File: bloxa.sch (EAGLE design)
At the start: 87 parts, among them CON1 PINHEAD_1X02-2.54, CON7 CON-4P-JST_GH-RA, CON8 CON-4P-JST_GH-RA, IC1 TPD3S014DBVR-SOT23-6, IC3 TJA1051, IC6 MCP9700, Q13 BUK9K6R2-40E,115, Q14 BUK9K6R2-40E,115, Q15 BUK9K6R2-40E,115

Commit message: updates
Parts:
- removed PAD42, PAD43: PAD-4X2, PADS:PAD-4X2
- added BAT+, BAT-: PAD-4X2, PADS:PAD-4X2
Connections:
- removed net CAN2_LED1: R9.1
- removed net LED_BLUE: R11.2
- removed net LED_GREEN: R12.2
- removed net LED_RED: R13.2
- removed net N$3: D1.C, D2.C, PAD43.P$1
- net CAN1_LED: now also R9.1
- net GPIO1: now also CON1.2
- net PGND: now also BAT-.P$1, CON1.1; no longer PAD42.P$1
- net RGB_LED_B: now also R11.2
- net RGB_LED_G: now also R12.2
- net RGB_LED_R: now also R13.2
- net VDC: now also BAT+.P$1, D1.C, D2.C
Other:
- note removed: "A bulk capacitor is required (not shown on this schematic). Its exact capacitance depends on the maximum power rating of the device."
- note removed: "Alternate smd pads"
- note removed: "HIGH SIDE INTERFACES"
- note removed: "In case CAN2 is not used leave pins CAN2_TX CAN2_RX floating"
- note removed: "In case POWER_ENABLE_IN is not used, leave it floating"
- note removed: "LOW SIDE INTERFACES"
- note removed: "Place ground and power ground junction as close to negative supply pad as possible"
- note removed: "STM32F446RET7 with operating temperature range -40°C ~ 105°C is not in stock on DIGIKEY (497-16775-ND)"
- moved on the sheet: A, B, C, C1, C11, C15, C16, C17, C18, C2, C21, C22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

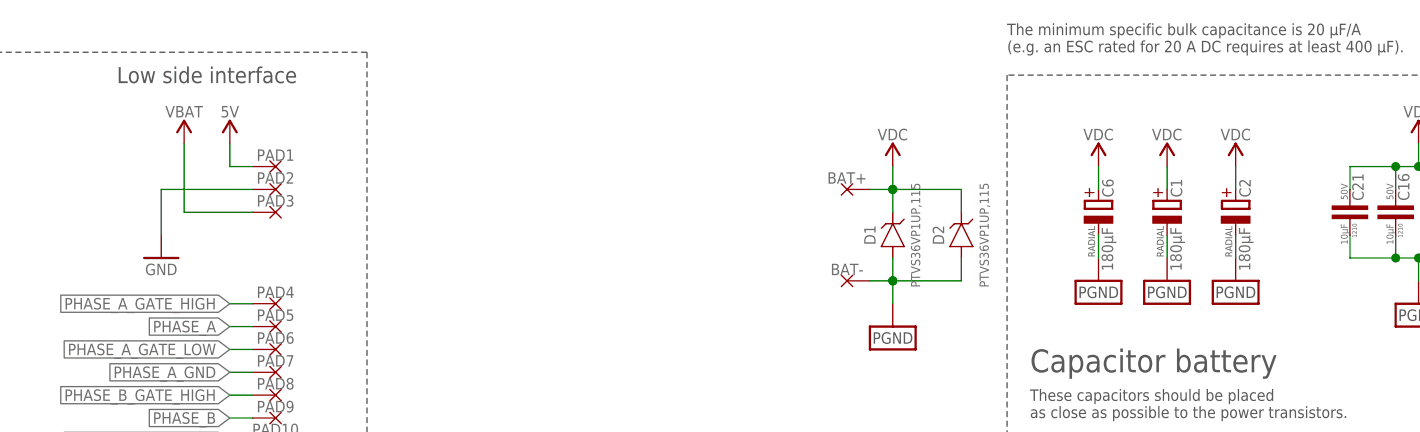
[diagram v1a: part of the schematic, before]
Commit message: proper DRC and some polygons
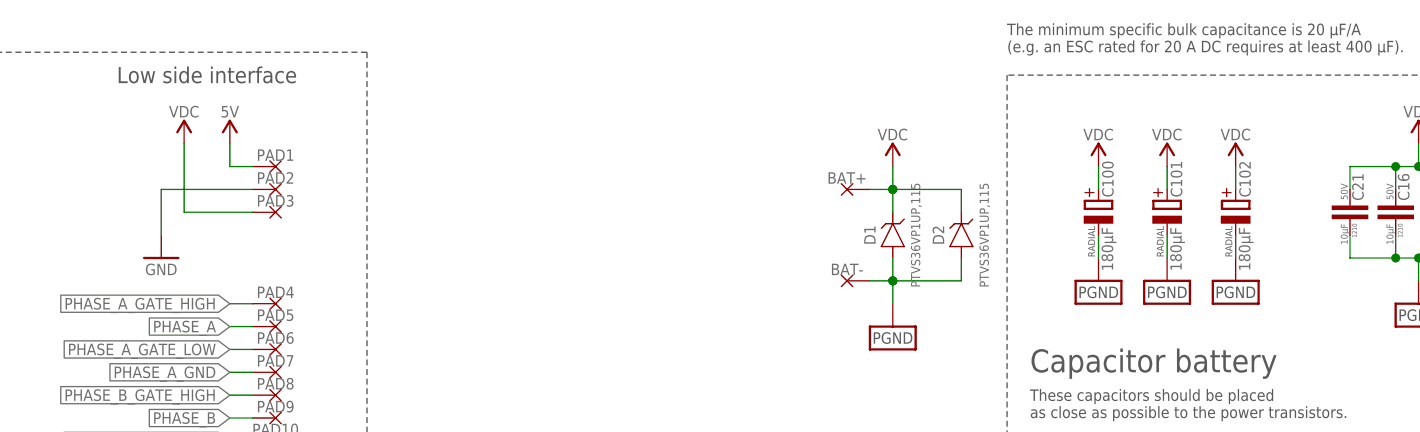
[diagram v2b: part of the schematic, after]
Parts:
- renumbered C1 to C101, C2 to C102, C6 to C100
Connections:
- removed net VBAT: PAD3.P$1
- net VDC: now also PAD3.P$1
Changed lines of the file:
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@@
 </attributes>
 <variantdefs>
-<variantdef name="Basic"/>
+<variantdef name="Basic" current="yes"/>
 </variantdefs>
 <classes>
@@
 </classes>
 <parts>
-<part name="+P15" library="supply_symbols" library_urn="urn:adsk.eagle:library:5017758" deviceset="VBAT" device=""/>
 <part name="+P16" library="supply_symbols" library_urn="urn:adsk.eagle:library:5017758" deviceset="5V" device=""/>
 <part name="GND17" library="supply_symbols" library_urn="urn:adsk.eagle:library:5017758" deviceset="GND" device="" value="GND"/>
@@
 <part name="D1" library="TVS_diodes" library_urn="urn:adsk.eagle:library:3333632" deviceset="PTVS36VP1UP,115" device="-SOD128" package3d_urn="urn:adsk.eagle:package:6533206/2" technology="-36V"/>
 <part name="D2" library="TVS_diodes" library_urn="urn:adsk.eagle:library:3333632" deviceset="PTVS36VP1UP,115" device="-SOD128" package3d_urn="urn:adsk.eagle:package:6533206/2" technology="-36V"/>
-<part name="C6" library="rc" library_urn="urn:adsk.eagle:library:2539423" deviceset="CPOL" device="-RADIAL_SIDE-8X21.5" package3d_urn="urn:adsk.eagle:package:7189333/2" value="180µF"/>
-<part name="C1" library="rc" library_urn="urn:adsk.eagle:library:2539423" deviceset="CPOL" device="-RADIAL_SIDE-8X21.5" package3d_urn="urn:adsk.eagle:package:7189333/2" value="180µF"/>
+<part name="C100" library="rc" library_urn="urn:adsk.eagle:library:2539423" deviceset="CPOL" device="-RADIAL_SIDE-8X21.5" package3d_urn="urn:adsk.eagle:package:7189333/2" value="180µF">
+<variant name="Basic" populate="no"/>
+</part>
+<part name="C101" library="rc" library_urn="urn:adsk.eagle:library:2539423" deviceset="CPOL" device="-RADIAL_SIDE-8X21.5" package3d_urn="urn:adsk.eagle:package:7189333/2" value="180µF">
+<variant name="Basic" populate="no"/>
+</part>
 <part name="GND2" library="supply_symbols" library_urn="urn:adsk.eagle:library:5017758" deviceset="PGND" device="" value="PGND"/>
 <part name="+P2" library="supply_symbols" library_urn="urn:adsk.eagle:library:5017758" deviceset="VDC" device=""/>
-<part name="C2" library="rc" library_urn="urn:adsk.eagle:library:2539423" deviceset="CPOL" device="-RADIAL_SIDE-8X21.5" package3d_urn="urn:adsk.eagle:package:7189333/2" value="180µF"/>
+<part name="C102" library="rc" library_urn="urn:adsk.eagle:library:2539423" deviceset="CPOL" device="-RADIAL_SIDE-8X21.5" package3d_urn="urn:adsk.eagle:package:7189333/2" value="180µF">
+<variant name="Basic" populate="no"/>
+</part>
 <part name="CON1" library="pinhead" library_urn="urn:adsk.eagle:library:2540341" deviceset="PINHEAD_1X02" device="-2.54" package3d_urn="urn:adsk.eagle:package:2540385/2">
 <variant name="Basic" populate="no"/>
@@
 <part name="GND3" library="supply_symbols" library_urn="urn:adsk.eagle:library:5017758" deviceset="PGND" device="" value="PGND"/>
 <part name="+P5" library="supply_symbols" library_urn="urn:adsk.eagle:library:5017758" deviceset="VDC" device=""/>
+<part name="+P7" library="supply_symbols" library_urn="urn:adsk.eagle:library:5017758" deviceset="VDC" device=""/>
 </parts>
 <sheets>
@@
 </plain>
 <instances>
-<instance part="+P15" gate="G$1" x="40.64" y="238.76" smashed="yes">
-<attribute name="VALUE" x="40.64" y="242.316" size="1.27" layer="96" font="vector" ratio="15" align="center"/>
-</instance>
 <instance part="+P16" gate="G$1" x="45.72" y="238.76" smashed="yes">
 <attribute name="VALUE" x="45.72" y="242.316" size="1.27" layer="96" font="vector" ratio="15" align="center"/>
@@
 <attribute name="MANF#" x="129.54" y="228.6" size="1.016" layer="95" font="vector" ratio="15" rot="R90" align="center"/>
 </instance>
-<instance part="C6" gate="G$1" x="142.24" y="231.14" smashed="yes" rot="R90">
+<instance part="C100" gate="G$1" x="142.24" y="231.14" smashed="yes" rot="R90">
 <attribute name="NAME" x="143.2814" y="232.791" size="1.27" layer="95" font="vector" rot="R90" align="center-left"/>
 <attribute name="VALUE" x="143.2306" y="229.489" size="1.27" layer="96" font="vector" rot="R270" align="center-left"/>
 <attribute name="PACKAGE" x="141.478" y="229.616" size="0.762" layer="97" font="vector" rot="R90" align="center-right"/>
 </instance>
-<instance part="C1" gate="G$1" x="149.86" y="231.14" smashed="yes" rot="R90">
+<instance part="C101" gate="G$1" x="149.86" y="231.14" smashed="yes" rot="R90">
 <attribute name="NAME" x="150.9014" y="232.791" size="1.27" layer="95" font="vector" rot="R90" align="center-left"/>
 <attribute name="VALUE" x="150.8506" y="229.489" size="1.27" layer="96" font="vector" rot="R270" align="center-left"/>
@@
 <attribute name="VALUE" x="157.48" y="239.776" size="1.27" layer="96" font="vector" ratio="15" align="center"/>
 </instance>
-<instance part="C2" gate="G$1" x="157.48" y="231.14" smashed="yes" rot="R90">
+<instance part="C102" gate="G$1" x="157.48" y="231.14" smashed="yes" rot="R90">
 <attribute name="NAME" x="158.5214" y="232.791" size="1.27" layer="95" font="vector" rot="R90" align="center-left"/>
 <attribute name="VALUE" x="158.4706" y="229.489" size="1.27" layer="96" font="vector" rot="R270" align="center-left"/>
@@
 <instance part="+P5" gate="G$1" x="119.38" y="236.22" smashed="yes">
 <attribute name="VALUE" x="119.38" y="239.776" size="1.27" layer="96" font="vector" ratio="15" align="center"/>
+</instance>
+<instance part="+P7" gate="G$1" x="40.64" y="238.76" smashed="yes">
+<attribute name="VALUE" x="40.64" y="242.316" size="1.27" layer="96" font="vector" ratio="15" align="center"/>
 </instance>
 </instances>
@@
 <label x="45.72" y="172.72" size="1.27" layer="95" rot="R180" xref="yes"/>
 <pinref part="PAD20" gate="G$1" pin="P$1"/>
-</segment>
-</net>
-<net name="VBAT" class="1">
-<segment>
-<wire x1="48.26" y1="231.14" x2="40.64" y2="231.14" width="0.1524" layer="91"/>
-<pinref part="+P15" gate="G$1" pin="VBAT"/>
-<wire x1="40.64" y1="231.14" x2="40.64" y2="238.76" width="0.1524" layer="91"/>
-<pinref part="PAD3" gate="G$1" pin="P$1"/>
 </segment>
 </net>
@@
 <pinref part="GND37" gate="G$1" pin="PGND"/>
 <wire x1="142.24" y1="226.06" x2="142.24" y2="228.6" width="0.1524" layer="91"/>
-<pinref part="C6" gate="G$1" pin="-"/>
+<pinref part="C100" gate="G$1" pin="-"/>
 </segment>
 <segment>
 <pinref part="GND38" gate="G$1" pin="PGND"/>
 <wire x1="149.86" y1="226.06" x2="149.86" y2="228.6" width="0.1524" layer="91"/>
-<pinref part="C1" gate="G$1" pin="-"/>
+<pinref part="C101" gate="G$1" pin="-"/>
 </segment>
 <segment>
@@
 <pinref part="GND2" gate="G$1" pin="PGND"/>
 <wire x1="157.48" y1="226.06" x2="157.48" y2="228.6" width="0.1524" layer="91"/>
-<pinref part="C2" gate="G$1" pin="-"/>
+<pinref part="C102" gate="G$1" pin="-"/>
 </segment>
 <segment>
@@
 <wire x1="149.86" y1="236.22" x2="149.86" y2="233.68" width="0.1524" layer="91"/>
 <pinref part="+P19" gate="G$1" pin="VDC"/>
-<pinref part="C1" gate="G$1" pin="+"/>
+<pinref part="C101" gate="G$1" pin="+"/>
 </segment>
 <segment>
 <wire x1="142.24" y1="236.22" x2="142.24" y2="233.68" width="0.1524" layer="91"/>
 <pinref part="+P20" gate="G$1" pin="VDC"/>
-<pinref part="C6" gate="G$1" pin="+"/>
+<pinref part="C100" gate="G$1" pin="+"/>
 </segment>
 <segment>
@@
 <wire x1="157.48" y1="236.22" x2="157.48" y2="233.68" width="0.1524" layer="91"/>
 <pinref part="+P2" gate="G$1" pin="VDC"/>
-<pinref part="C2" gate="G$1" pin="+"/>
+<pinref part="C102" gate="G$1" pin="+"/>
 </segment>
 <segment>
@@
 <wire x1="119.38" y1="236.22" x2="119.38" y2="233.68" width="0.1524" layer="91"/>
 </segment>
-</net>
+<segment>
+<wire x1="48.26" y1="231.14" x2="40.64" y2="231.14" width="0.1524" layer="91"/>
+<wire x1="40.64" y1="231.14" x2="40.64" y2="238.76" width="0.1524" layer="91"/>
+<pinref part="PAD3" gate="G$1" pin="P$1"/>
+<pinref part="+P7" gate="G$1" pin="VDC"/>
+</segment>
+</net>

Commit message: some more progress
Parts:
- removed IC3: TJA1051, myxa_masterlib:TJA1051
- added IC2: TJA1051(X)/3-SO8, serial_interfaces:TJA1051(X)/3-SO8
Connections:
- removed net TEMP_SENS: PAD20.P$1
- new net N$2: IC2.S
- net CAN1_RX: now also IC2.RXD; no longer IC3.RXD
- net CAN1_TX: now also IC2.TXD; no longer IC3.TXD
- net GND: now also IC2.GND; no longer IC3.GND, IC3.S
- net N$22: now also IC2.CANH; no longer IC3.CANH
- net N$23: now also IC2.CANL; no longer IC3.CANL
- net TEMPERATURE_SENSOR: now also PAD20.P$1
- net VDD_5V: now also IC2.VCC, IC2.VIO; no longer IC3.VCC, IC3.VIO
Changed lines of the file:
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@@
 <variantdefs>
 <variantdef name="Basic"/>
-<variantdef name="nocaps" current="yes"/>
+<variantdef name="nocaps"/>
 </variantdefs>
 <classes>
@@
 <variant name="Basic" populate="no"/>
 </part>
-<part name="IC3" library="myxa_masterlib" library_urn="urn:adsk.eagle:library:1040030" deviceset="TJA1051" device="" package3d_urn="urn:adsk.eagle:package:1040194/3"/>
 <part name="C11" library="C_digikey" library_urn="urn:adsk.eagle:library:2539367" deviceset="0.1µF" device="-0402" package3d_urn="urn:adsk.eagle:package:2539379/2" technology="-16V_10%_X7R" value="0.1µF"/>
 <part name="GND24" library="supply_symbols" library_urn="urn:adsk.eagle:library:5017758" deviceset="GND" device="" value="GND"/>
@@
 <part name="+P5" library="supply_symbols" library_urn="urn:adsk.eagle:library:5017758" deviceset="VDC" device=""/>
 <part name="+P7" library="supply_symbols" library_urn="urn:adsk.eagle:library:5017758" deviceset="VDC" device=""/>
+<part name="IC2" library="serial_interfaces" library_urn="urn:adsk.eagle:library:4770999" deviceset="TJA1051(X)/3" device="-SO8" package3d_urn="urn:adsk.eagle:package:4771007/3"/>
 </parts>
 <sheets>
@@
 <attribute name="NAME" x="48.26" y="161.29" size="1.27" layer="95" font="vector" ratio="15" rot="MR0" align="center"/>
 </instance>
-<instance part="IC3" gate="G$1" x="322.58" y="116.84" smashed="yes">
-<attribute name="NAME" x="331.47" y="130.556" size="1.27" layer="95" font="vector" ratio="15" align="center"/>
-</instance>
 <instance part="C11" gate="G$1" x="294.64" y="116.84" smashed="yes" rot="R270">
 <attribute name="NAME" x="293.751" y="115.57" size="1.27" layer="95" rot="R270" align="center-left"/>
@@
 <attribute name="VALUE" x="40.64" y="242.316" size="1.27" layer="96" font="vector" ratio="15" align="center"/>
 </instance>
+<instance part="IC2" gate="G$1" x="322.58" y="116.84" smashed="yes">
+<attribute name="NAME" x="331.47" y="130.556" size="1.27" layer="95" font="vector" ratio="15" align="center"/>
+<attribute name="MANF#" x="331.47" y="115.824" size="1.27" layer="95" font="vector" ratio="15" align="center"/>
+</instance>
 </instances>
 <busses>
@@
 </segment>
 <segment>
-<pinref part="IC3" gate="G$1" pin="TXD"/>
 <wire x1="320.04" y1="127" x2="317.5" y2="127" width="0.1524" layer="91"/>
 <wire x1="317.5" y1="127" x2="314.96" y2="127" width="0.1524" layer="91"/>
 <label x="314.96" y="127" size="1.27" layer="95" rot="R180" xref="yes"/>
+<pinref part="IC2" gate="G$1" pin="TXD"/>
 </segment>
 </net>
@@
 <wire x1="363.22" y1="152.4" x2="360.68" y2="152.4" width="0.1524" layer="91"/>
 <label x="360.68" y="152.4" size="1.27" layer="95" rot="MR0" xref="yes"/>
-</segment>
-</net>
-<net name="TEMP_SENS" class="0">
-<segment>
-<wire x1="48.26" y1="172.72" x2="45.72" y2="172.72" width="0.1524" layer="91"/>
-<label x="45.72" y="172.72" size="1.27" layer="95" rot="R180" xref="yes"/>
-<pinref part="PAD20" gate="G$1" pin="P$1"/>
 </segment>
 </net>
@@
 </segment>
 <segment>
-<pinref part="IC3" gate="G$1" pin="RXD"/>
 <wire x1="320.04" y1="119.38" x2="314.96" y2="119.38" width="0.1524" layer="91"/>
 <label x="314.96" y="119.38" size="1.27" layer="95" rot="R180" xref="yes"/>
+<pinref part="IC2" gate="G$1" pin="RXD"/>
 </segment>
 </net>
@@
 </segment>
 <segment>
-<pinref part="IC3" gate="G$1" pin="VCC"/>
 <pinref part="C11" gate="G$1" pin="1"/>
 <wire x1="320.04" y1="121.92" x2="299.72" y2="121.92" width="0.1524" layer="91"/>
@@
 <junction x="294.64" y="121.92"/>
 <pinref part="+P13" gate="G$1" pin="VDD_5V"/>
-<pinref part="IC3" gate="G$1" pin="VIO"/>
 <wire x1="342.9" y1="119.38" x2="345.44" y2="119.38" width="0.1524" layer="91"/>
 <wire x1="345.44" y1="119.38" x2="345.44" y2="111.76" width="0.1524" layer="91"/>
@@
 <wire x1="299.72" y1="111.76" x2="299.72" y2="121.92" width="0.1524" layer="91"/>
 <junction x="299.72" y="121.92"/>
+<pinref part="IC2" gate="G$1" pin="VCC"/>
+<pinref part="IC2" gate="G$1" pin="VIO"/>
 </segment>
 <segment>
@@
 </segment>
 <segment>
-<pinref part="IC3" gate="G$1" pin="GND"/>
 <wire x1="320.04" y1="124.46" x2="317.5" y2="124.46" width="0.1524" layer="91"/>
 <wire x1="317.5" y1="124.46" x2="317.5" y2="116.84" width="0.1524" layer="91"/>
 <pinref part="GND24" gate="1" pin="GND"/>
+<pinref part="IC2" gate="G$1" pin="GND"/>
 </segment>
 <segment>
@@
 <pinref part="C11" gate="G$1" pin="2"/>
 <wire x1="294.64" y1="109.22" x2="294.64" y2="114.3" width="0.1524" layer="91"/>
-</segment>
-<segment>
-<pinref part="IC3" gate="G$1" pin="S"/>
-<wire x1="342.9" y1="127" x2="350.52" y2="127" width="0.1524" layer="91"/>
-<pinref part="GND29" gate="1" pin="GND"/>
-<wire x1="350.52" y1="127" x2="350.52" y2="116.84" width="0.1524" layer="91"/>
 </segment>
 <segment>
@@
 <label x="160.02" y="182.88" size="1.27" layer="95" rot="R180" xref="yes"/>
 </segment>
+<segment>
+<wire x1="48.26" y1="172.72" x2="45.72" y2="172.72" width="0.1524" layer="91"/>
+<label x="45.72" y="172.72" size="1.27" layer="95" rot="R180" xref="yes"/>
+<pinref part="PAD20" gate="G$1" pin="P$1"/>
+</segment>
 </net>
 <net name="PGND" class="0">
@@
 <wire x1="358.14" y1="101.6" x2="363.22" y2="101.6" width="0.1524" layer="91"/>
 <wire x1="355.6" y1="124.46" x2="347.98" y2="124.46" width="0.1524" layer="91"/>
-<pinref part="IC3" gate="G$1" pin="CANH"/>
 <wire x1="347.98" y1="124.46" x2="342.9" y2="124.46" width="0.1524" layer="91"/>
 <pinref part="CON7" gate="G$1" pin="2"/>
@@
 <wire x1="358.14" y1="101.6" x2="358.14" y2="124.46" width="0.1524" layer="91"/>
 <junction x="358.14" y="124.46"/>
+<pinref part="IC2" gate="G$1" pin="CANH"/>
 </segment>
 </net>
@@
 <pinref part="CON8" gate="G$1" pin="3"/>
 <wire x1="355.6" y1="99.06" x2="363.22" y2="99.06" width="0.1524" layer="91"/>
-<pinref part="IC3" gate="G$1" pin="CANL"/>
 <wire x1="342.9" y1="121.92" x2="347.98" y2="121.92" width="0.1524" layer="91"/>
 <wire x1="347.98" y1="121.92" x2="355.6" y2="121.92" width="0.1524" layer="91"/>
@@
 <wire x1="355.6" y1="99.06" x2="355.6" y2="121.92" width="0.1524" layer="91"/>
 <junction x="355.6" y="121.92"/>
+<pinref part="IC2" gate="G$1" pin="CANL"/>
 </segment>
 </net>
@@
 </segment>
 </net>
+<net name="N$2" class="0">
+<segment>
+<wire x1="342.9" y1="127" x2="350.52" y2="127" width="0.1524" layer="91"/>
+<pinref part="GND29" gate="1" pin="GND"/>
+<wire x1="350.52" y1="127" x2="350.52" y2="116.84" width="0.1524" layer="91"/>
+<pinref part="IC2" gate="G$1" pin="S"/>
+</segment>
+</net>

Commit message: some progress
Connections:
- net GND: no longer PAD2.P$1
- net PGND: now also PAD2.P$1
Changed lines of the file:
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@@
 <parts>
 <part name="+P16" library="supply_symbols" library_urn="urn:adsk.eagle:library:5017758" deviceset="5V" device=""/>
-<part name="GND17" library="supply_symbols" library_urn="urn:adsk.eagle:library:5017758" deviceset="GND" device="" value="GND"/>
 <part name="PAD1" library="PADS" library_urn="urn:adsk.eagle:library:3188696" deviceset="PAD" device="-1X1.5" value="PAD-1X1.5">
 <variant name="Basic" populate="no"/>
@@
 <part name="+P7" library="supply_symbols" library_urn="urn:adsk.eagle:library:5017758" deviceset="VDC" device=""/>
 <part name="IC2" library="serial_interfaces" library_urn="urn:adsk.eagle:library:4770999" deviceset="TJA1051(X)/3" device="-SO8" package3d_urn="urn:adsk.eagle:package:4771007/3"/>
+<part name="GND4" library="supply_symbols" library_urn="urn:adsk.eagle:library:5017758" deviceset="PGND" device="" value="PGND"/>
 </parts>
 <sheets>
@@
 <attribute name="VALUE" x="45.72" y="242.316" size="1.27" layer="96" font="vector" ratio="15" align="center"/>
 </instance>
-<instance part="GND17" gate="1" x="38.1" y="226.06" smashed="yes">
-<attribute name="VALUE" x="38.1" y="224.79" size="1.27" layer="96" font="vector" ratio="15" align="center"/>
-</instance>
 <instance part="PAD1" gate="G$1" x="50.8" y="236.22" smashed="yes" rot="MR0">
 <attribute name="NAME" x="50.8" y="237.49" size="1.27" layer="95" font="vector" ratio="15" rot="MR0" align="center"/>
@@
 <attribute name="NAME" x="331.47" y="130.556" size="1.27" layer="95" font="vector" ratio="15" align="center"/>
 <attribute name="MANF#" x="331.47" y="115.824" size="1.27" layer="95" font="vector" ratio="15" align="center"/>
+</instance>
+<instance part="GND4" gate="G$1" x="38.1" y="228.6" smashed="yes">
+<attribute name="VALUE" x="38.1" y="227.33" size="1.27" layer="97" font="vector" ratio="15" align="center"/>
 </instance>
 </instances>
@@
 </net>
 <net name="GND" class="0">
-<segment>
-<pinref part="GND17" gate="1" pin="GND"/>
-<wire x1="48.26" y1="233.68" x2="38.1" y2="233.68" width="0.1524" layer="91"/>
-<wire x1="38.1" y1="233.68" x2="38.1" y2="228.6" width="0.1524" layer="91"/>
-<pinref part="PAD2" gate="G$1" pin="P$1"/>
-</segment>
 <segment>
 <wire x1="320.04" y1="124.46" x2="317.5" y2="124.46" width="0.1524" layer="91"/>
@@
 <junction x="177.8" y="226.06"/>
 </segment>
-</net>
+<segment>
+<wire x1="48.26" y1="233.68" x2="38.1" y2="233.68" width="0.1524" layer="91"/>
+<pinref part="PAD2" gate="G$1" pin="P$1"/>
+<pinref part="GND4" gate="G$1" pin="PGND"/>
+<wire x1="38.1" y1="231.14" x2="38.1" y2="233.68" width="0.1524" layer="91"/>
+</segment>
+</net>
